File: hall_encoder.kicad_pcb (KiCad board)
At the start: 2 copper layers, 50 x 22 mm, 30 parts, among them J1 Conn_02x03_Odd_Even, J2 Conn_01x04, J3 Conn_01x04, J4 Conn_01x02, J5 Conn_01x02, J6 Conn_01x02, SW1 RESET, U1 AP2210, U2 STM32F042F4Px, U3 MA730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

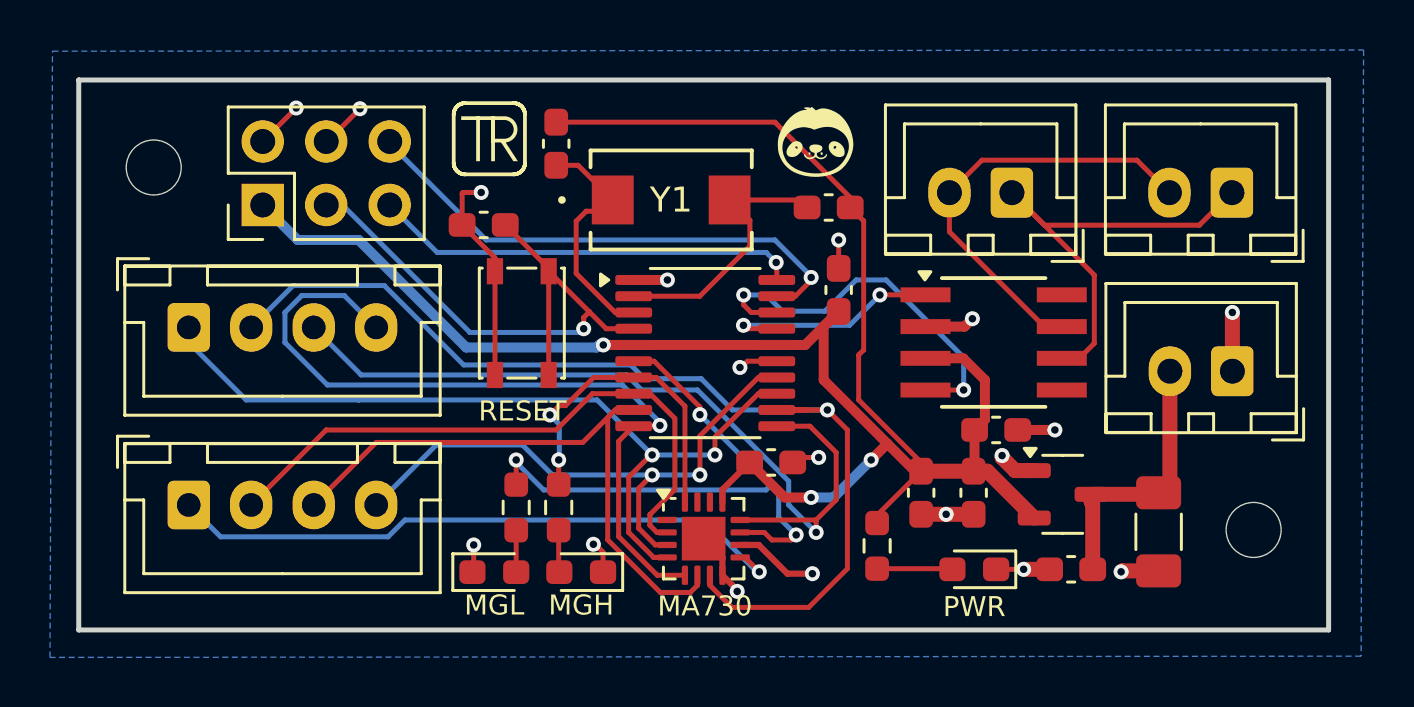
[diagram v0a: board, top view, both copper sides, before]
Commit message: Remove all can components
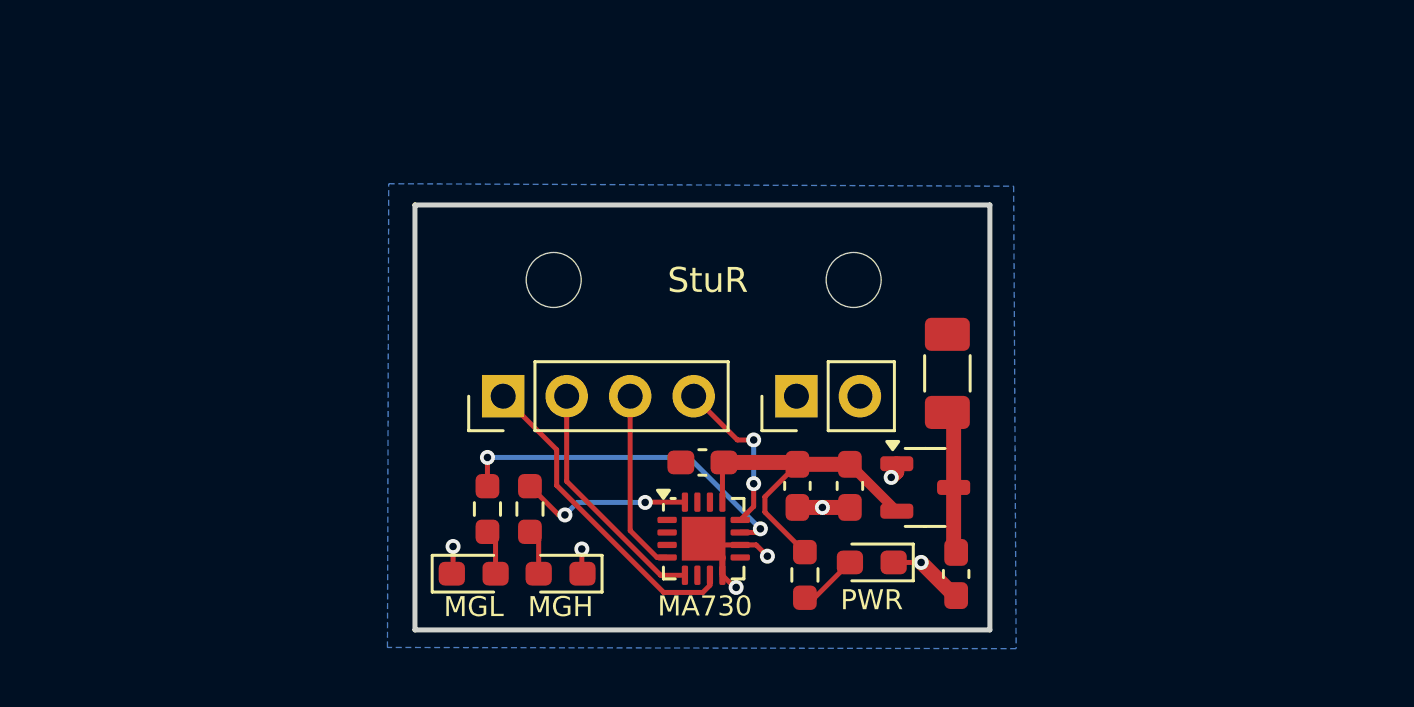
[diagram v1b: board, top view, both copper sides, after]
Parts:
- removed C10, C4, C7: 100nF, Capacitor_SMD:C_0603_1608Metric_Pad1.08x0.95mm_HandSolder
- removed C5, C6: 20pF, Capacitor_SMD:C_0603_1608Metric_Pad1.08x0.95mm_HandSolder
- removed J1: Conn_02x03_Odd_Even, Connector_PinHeader_2.54mm:PinHeader_2x03_P2.54mm_Vertical
- removed J2: Conn_01x04, Connector_JST:JST_XH_B4B-XH-A_1x04_P2.50mm_Vertical
- removed J4, J5: Conn_01x02, Connector_JST:JST_XH_B2B-XH-A_1x02_P2.50mm_Vertical
- removed SW1: RESET, Button_Switch_SMD:SW_SPST_PTS810
- removed U2: STM32F042F4Px, Package_SO:TSSOP-20_4.4x6.5mm_P0.65mm
- removed U4: TCAN332, Package_SO:PowerIntegrations_SO-8
- removed Y1: 8 MHz, ECS-080-18-23G-JGN-TR:XTAL_ECS-23G_6P0X3P5X1P2_ECS-L
- J3: footprint Connector_JST:JST_XH_B4B-XH-A_1x04_P2.50mm_Vertical -> Connector_PinHeader_2.54mm:PinHeader_1x04_P2.54mm_Vertical
- J6: footprint Connector_JST:JST_XH_B2B-XH-A_1x02_P2.50mm_Vertical -> Connector_PinHeader_2.54mm:PinHeader_1x02_P2.54mm_Vertical
- moved H2 18.9 mm to (156.0, 71.0)
- moved J6 17.5 mm to (153.7, 75.7), turned to 90 degrees
- moved H1 16.6 mm to (144.0, 71.0)
- moved J3 12.9 mm to (142.0, 75.7), turned to 90 degrees
- moved C2 10.6 mm to (159.8, 74.7), turned to 90 degrees
- moved U1 5.51 mm to (158.9, 79.3)
- moved C3 4.96 mm to (155.8, 79.2)
- moved C9 4.96 mm to (153.8, 79.2)
- moved C1 4.60 mm to (160.1, 82.8), turned to -90 degrees
- moved D1 4.11 mm to (156.7, 82.3)
- moved R1 3.11 mm to (154.1, 82.8)
- moved C8 2.75 mm to (149.9, 78.3), turned to 180 degrees
- moved R3 1.15 mm to (141.3, 80.2)
- moved R2 1.15 mm to (143.1, 80.2)
- moved D2 0.83 mm to (144.3, 82.8)
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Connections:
- net MGH renamed Net-(U3-MGH)
- net MGL renamed Net-(U3-MGL)
- J3 pad 1: MOSI -> MISO
- J3 pad 2: MISO -> CS
- J3 pad 3: CLK -> MOSI
- J3 pad 4: CS -> CLK
- U3 pad 2: A -> unconnected-(U3-A-Pad2)
- U3 pad 3: Z -> unconnected-(U3-Z-Pad3)
- U3 pad 6: B -> unconnected-(U3-B-Pad6)
- U3 pad 9: PWM -> unconnected-(U3-PWM-Pad9)
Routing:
- net +3.3V: track 83.4 -> 14.5 mm, vias 3 -> 0
- net MISO: track 42.7 -> 12.9 mm, vias 1 -> 0
- net CLK: track 33.4 -> 6.55 mm, vias 1 -> 2
- net GND: track 39.5 -> 13.6 mm, vias 18 -> 7
- net MOSI: track 32.9 -> 7.30 mm, vias 2 -> 0
- net PWM: track 25.5 -> 0.00 mm, vias 1 -> 0
- net A: track 24.7 -> 0.00 mm
- net B: track 24.7 -> 0.00 mm
- net NRST: track 24.3 -> 0.00 mm, vias 1 -> 0
- net Z: track 23.8 -> 0.00 mm, vias 2 -> 0
- net CS: track 31.1 -> 9.69 mm, vias 1 -> 0
- net SWDIO: track 20.9 -> 0.00 mm, vias 1 -> 0
- net CANL: track 18.8 -> 0.00 mm
- net CANH: track 17.5 -> 0.00 mm
- net SWCLK: track 17.1 -> 0.00 mm, vias 1 -> 0
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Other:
- board size 50 x 22 mm -> 23 x 17 mm
- board text added: "StuR"
